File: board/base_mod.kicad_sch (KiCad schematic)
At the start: 31 parts, among them J3 RS-232, J4 LCD, Q5 BC548, Q6 BC548, SW10 MENU, SW3 RI, SW4 UP, SW5 LE, SW6 OK, SW7 DN, SW8 CANCEL, SW9 BACK, U4 AT24C1024B, U5 MAX3232, U6 24LCxxx, U7 MCP23008-xP, U8 BOB-12009

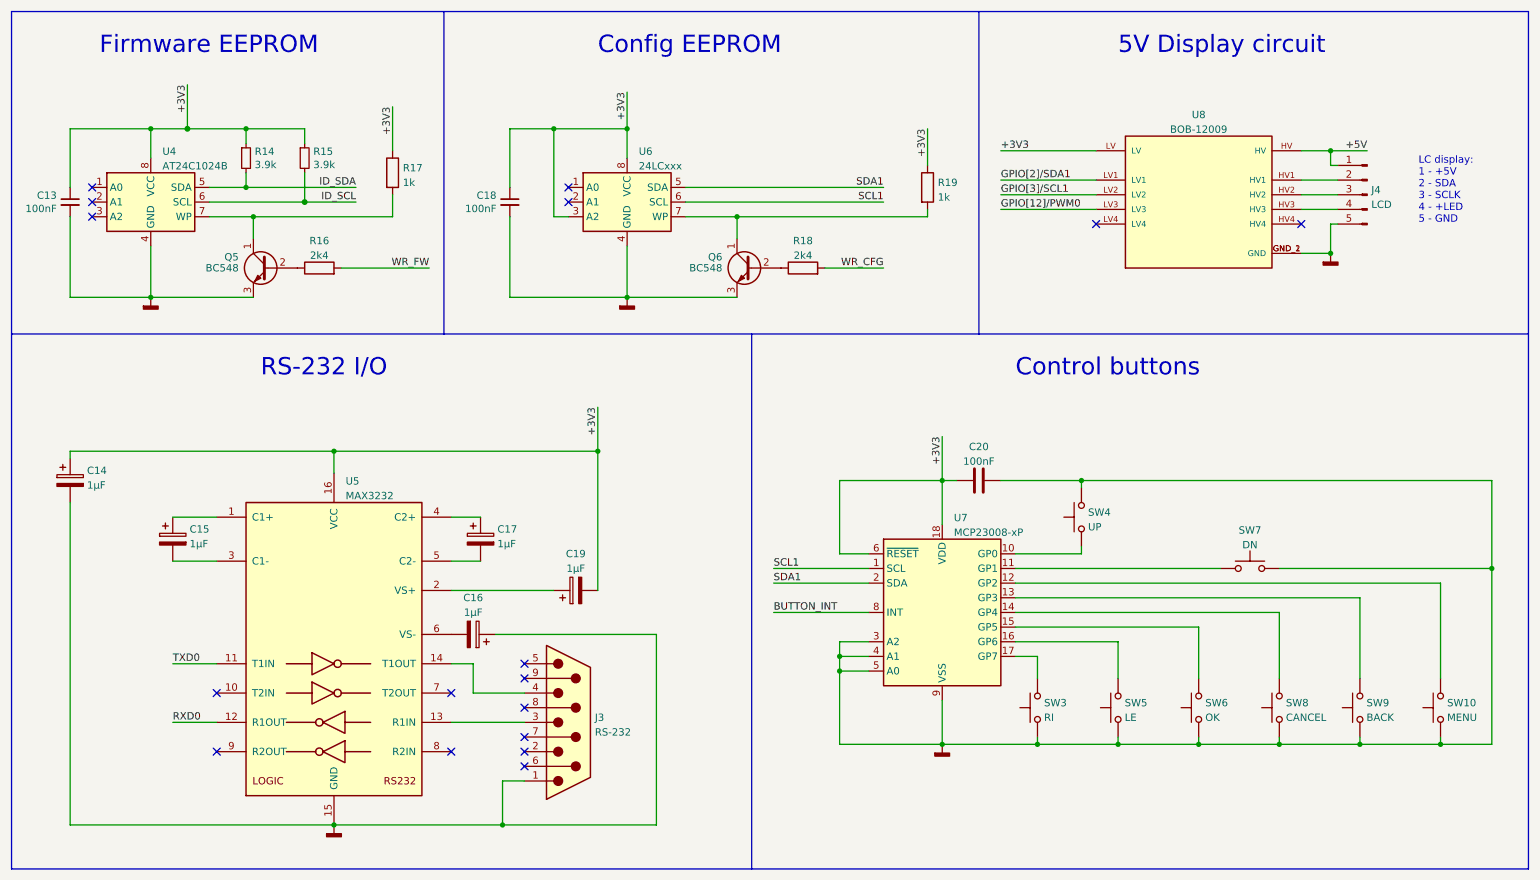
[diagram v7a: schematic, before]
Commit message: Make it a multiboard project.
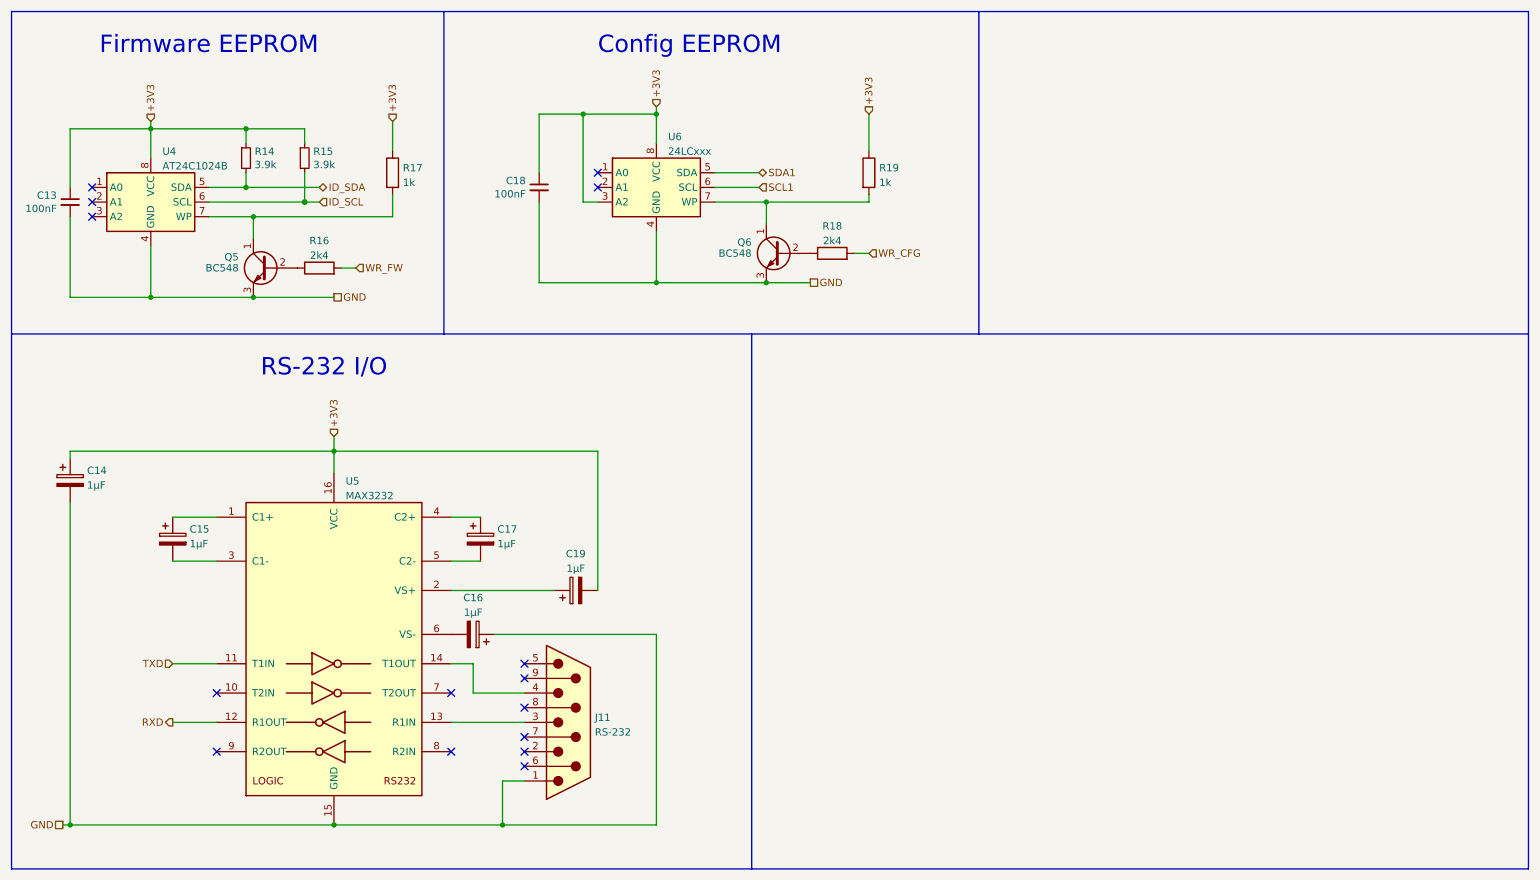
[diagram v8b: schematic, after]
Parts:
- removed C20: 100nF, Capacitor_THT:C_Disc_D5.0mm_W2.5mm_P5.00mm, symbol Device:C
- removed J4: LCD, Connector_PinHeader_2.54mm:PinHeader_1x05_P2.54mm_Vertical_SMD_Pin1Right, symbol Connector:Conn_01x05_Male
- removed SW10: MENU, Button_Switch_THT:SW_PUSH_6mm, symbol Switch:SW_Push
- removed SW3: RI, Button_Switch_THT:SW_PUSH_6mm, symbol Switch:SW_Push
- removed SW4: UP, Button_Switch_THT:SW_PUSH_6mm, symbol Switch:SW_Push
- removed SW5: LE, Button_Switch_THT:SW_PUSH_6mm, symbol Switch:SW_Push
- removed SW6: OK, Button_Switch_THT:SW_PUSH_6mm, symbol Switch:SW_Push
- removed SW7: DN, Button_Switch_THT:SW_PUSH_6mm, symbol Switch:SW_Push
- removed SW8: CANCEL, Button_Switch_THT:SW_PUSH_6mm, symbol Switch:SW_Push
- removed SW9: BACK, Button_Switch_THT:SW_PUSH_6mm, symbol Switch:SW_Push
- removed U7: MCP23008-xP, Package_DIP:DIP-18_W7.62mm, symbol Interface_Expansion:MCP23008-xP
- removed U8: BOB-12009, BOB-12009:CONV_BOB-12009, symbol BOB-12009:BOB-12009
- renumbered J3 to J11
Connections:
- net GNDD renamed GND
- net RXD0 renamed RXD
- net TXD0 renamed TXD
- no-connect marks 17 -> 15
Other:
- note removed: "5V Display circuit"
- note removed: "Control buttons"
- note removed: "LC display: 1 - +5V 2 - SDA 3 - SCLK 4 - +LED 5 - GND"
- moved on the sheet: C18, Q6, R18, R19, U6
